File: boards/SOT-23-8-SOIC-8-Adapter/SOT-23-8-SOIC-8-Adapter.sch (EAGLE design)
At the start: 5 parts, among them J1 PINHD-1X4, J2 PINHD-1X4, Q1 LTC4365, Q2 IRLML2060TRPBF, Q3 IRLML2060TRPBF

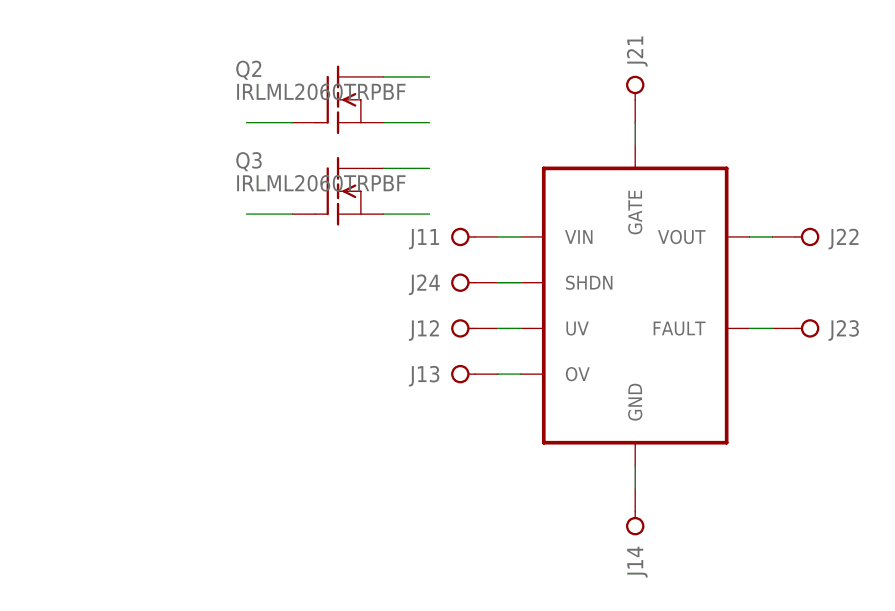
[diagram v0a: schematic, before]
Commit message: Fixed SOT-23-8 adapter to have right footprint, and added SOIC-8
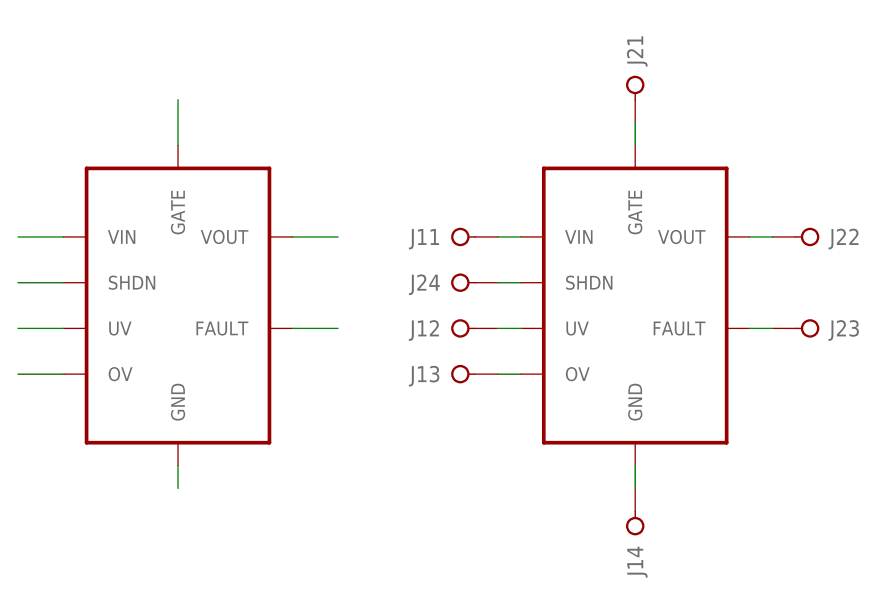
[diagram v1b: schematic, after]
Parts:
- removed Q2, Q3: IRLML2060TRPBF, SaintGimp:IRLML2060TRPBF
- added U$1: DUMMY1, SaintGimp:DUMMY1
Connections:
- net 1-1: now also U$1.VIN; no longer Q2.SRC
- net 1-2: now also U$1.UV; no longer Q2.GATE
- net 1-3: now also U$1.OV; no longer Q3.SRC
- net 1-4: now also U$1.GND; no longer Q3.GATE
- net 2-1: now also U$1.GATE; no longer Q2.DRN
- net 2-2: now also U$1.VOUT
- net 2-3: now also U$1.FAULT
- net 2-4: now also U$1.SHDN; no longer Q3.DRN
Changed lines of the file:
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@@
 <layer number="56" name="wert" color="7" fill="1" visible="no" active="no"/>
 <layer number="57" name="tCAD" color="7" fill="1" visible="no" active="no"/>
+<layer number="59" name="tCarbon" color="7" fill="1" visible="no" active="no"/>
+<layer number="60" name="bCarbon" color="7" fill="1" visible="no" active="no"/>
 <layer number="90" name="Modules" color="5" fill="1" visible="yes" active="yes"/>
 <layer number="91" name="Nets" color="2" fill="1" visible="yes" active="yes"/>
@@
 <layer number="127" name="_tValues" color="7" fill="1" visible="yes" active="yes"/>
 <layer number="128" name="_bValues" color="7" fill="1" visible="yes" active="yes"/>
+<layer number="129" name="Mask" color="7" fill="1" visible="yes" active="yes"/>
 <layer number="131" name="tAdjust" color="7" fill="1" visible="no" active="yes"/>
 <layer number="132" name="bAdjust" color="7" fill="1" visible="no" active="yes"/>
@@
 <part name="J1" library="SaintGimp" deviceset="PINHD-1X4" device=""/>
 <part name="J2" library="SaintGimp" deviceset="PINHD-1X4" device=""/>
-<part name="Q2" library="SaintGimp" deviceset="IRLML2060TRPBF" device=""/>
-<part name="Q3" library="SaintGimp" deviceset="IRLML2060TRPBF" device=""/>
+<part name="U$1" library="SaintGimp" deviceset="DUMMY1" device=""/>
 </parts>
 <sheets>
@@
 <instance part="J2" gate="3" x="83.82" y="48.26" rot="R180"/>
 <instance part="J2" gate="4" x="43.18" y="53.34"/>
-<instance part="Q2" gate="G$1" x="30.48" y="73.66"/>
-<instance part="Q3" gate="G$1" x="30.48" y="63.5"/>
+<instance part="U$1" gate="G$1" x="12.7" y="50.8"/>
 </instances>
 <busses>
@@
 </segment>
 <segment>
-<pinref part="Q2" gate="G$1" pin="SRC"/>
-<wire x1="35.56" y1="71.12" x2="40.64" y2="71.12" width="0.1524" layer="91"/>
+<pinref part="U$1" gate="G$1" pin="VIN"/>
+<wire x1="0" y1="58.42" x2="-5.08" y2="58.42" width="0.1524" layer="91"/>
 </segment>
 </net>
@@
 </segment>
 <segment>
-<pinref part="Q2" gate="G$1" pin="GATE"/>
-<wire x1="25.4" y1="71.12" x2="20.32" y2="71.12" width="0.1524" layer="91"/>
+<pinref part="U$1" gate="G$1" pin="UV"/>
+<wire x1="0" y1="48.26" x2="-5.08" y2="48.26" width="0.1524" layer="91"/>
 </segment>
 </net>
@@
 </segment>
 <segment>
-<pinref part="Q3" gate="G$1" pin="SRC"/>
-<wire x1="35.56" y1="60.96" x2="40.64" y2="60.96" width="0.1524" layer="91"/>
+<pinref part="U$1" gate="G$1" pin="OV"/>
+<wire x1="0" y1="43.18" x2="-5.08" y2="43.18" width="0.1524" layer="91"/>
 </segment>
 </net>
@@
 </segment>
 <segment>
-<pinref part="Q3" gate="G$1" pin="GATE"/>
-<wire x1="25.4" y1="60.96" x2="20.32" y2="60.96" width="0.1524" layer="91"/>
+<pinref part="U$1" gate="G$1" pin="GND"/>
+<wire x1="12.7" y1="33.02" x2="12.7" y2="30.48" width="0.1524" layer="91"/>
 </segment>
 </net>
@@
 </segment>
 <segment>
-<pinref part="Q2" gate="G$1" pin="DRN"/>
-<wire x1="35.56" y1="76.2" x2="40.64" y2="76.2" width="0.1524" layer="91"/>
+<pinref part="U$1" gate="G$1" pin="GATE"/>
+<wire x1="12.7" y1="68.58" x2="12.7" y2="73.66" width="0.1524" layer="91"/>
 </segment>
 </net>
@@
 <wire x1="78.74" y1="58.42" x2="76.2" y2="58.42" width="0.1524" layer="91"/>
 </segment>
+<segment>
+<pinref part="U$1" gate="G$1" pin="VOUT"/>
+<wire x1="25.4" y1="58.42" x2="30.48" y2="58.42" width="0.1524" layer="91"/>
+</segment>
 </net>
 <net name="2-3" class="0">
@@
 <wire x1="78.74" y1="48.26" x2="76.2" y2="48.26" width="0.1524" layer="91"/>
 </segment>
+<segment>
+<pinref part="U$1" gate="G$1" pin="FAULT"/>
+<wire x1="25.4" y1="48.26" x2="30.48" y2="48.26" width="0.1524" layer="91"/>
+</segment>
 </net>
 <net name="2-4" class="0">
@@
 </segment>
 <segment>
-<pinref part="Q3" gate="G$1" pin="DRN"/>
-<wire x1="35.56" y1="66.04" x2="40.64" y2="66.04" width="0.1524" layer="91"/>
-</segment>
-</net>
+<pinref part="U$1" gate="G$1" pin="SHDN"/>
+<wire x1="0" y1="53.34" x2="-5.08" y2="53.34" width="0.1524" layer="91"/>
+</segment>
+</net>
